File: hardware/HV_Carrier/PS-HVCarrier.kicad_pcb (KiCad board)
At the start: 2 copper layers, 291 parts, among them IC1 LM74502DDFR, IC2 TCAN3413DR, IC3 TCAN3413DR, J1 Shunt Breakout, J10 Shunt Conn, J12 Discharge Vin, J13 Charge Vin, J2 Hall Breakout, J3 IMD_Conn, J4 Voltage Tap, J5 BPS Conn, J6 USB_C_Receptacle_USB2.0_16P, J7 SWD_Header, J8 SWD, J9 LZSR 80-P, Q1 PSMN012-100YS, Q2 PSMN012-100YS, SW1 Reset, SW2 SW_SPDT, U1 MCP1826S, U10 TPS2117DRLR, U11 TLV9002QDRQ1, U12 TLV9002QDRQ1, U13 LMR51635XDDCR, U2 CDSOT23-T24CAN, U3 CDSOT23-T24CAN, U4 AMC3311QDWERQ1, U5 STM32G473CETx, U6 TLV9002QDRQ1, U7 AMC3311QDWERQ1, U8 AMC3311QDWERQ1, U9 AMC3311QDWERQ1, Y1 Crystal

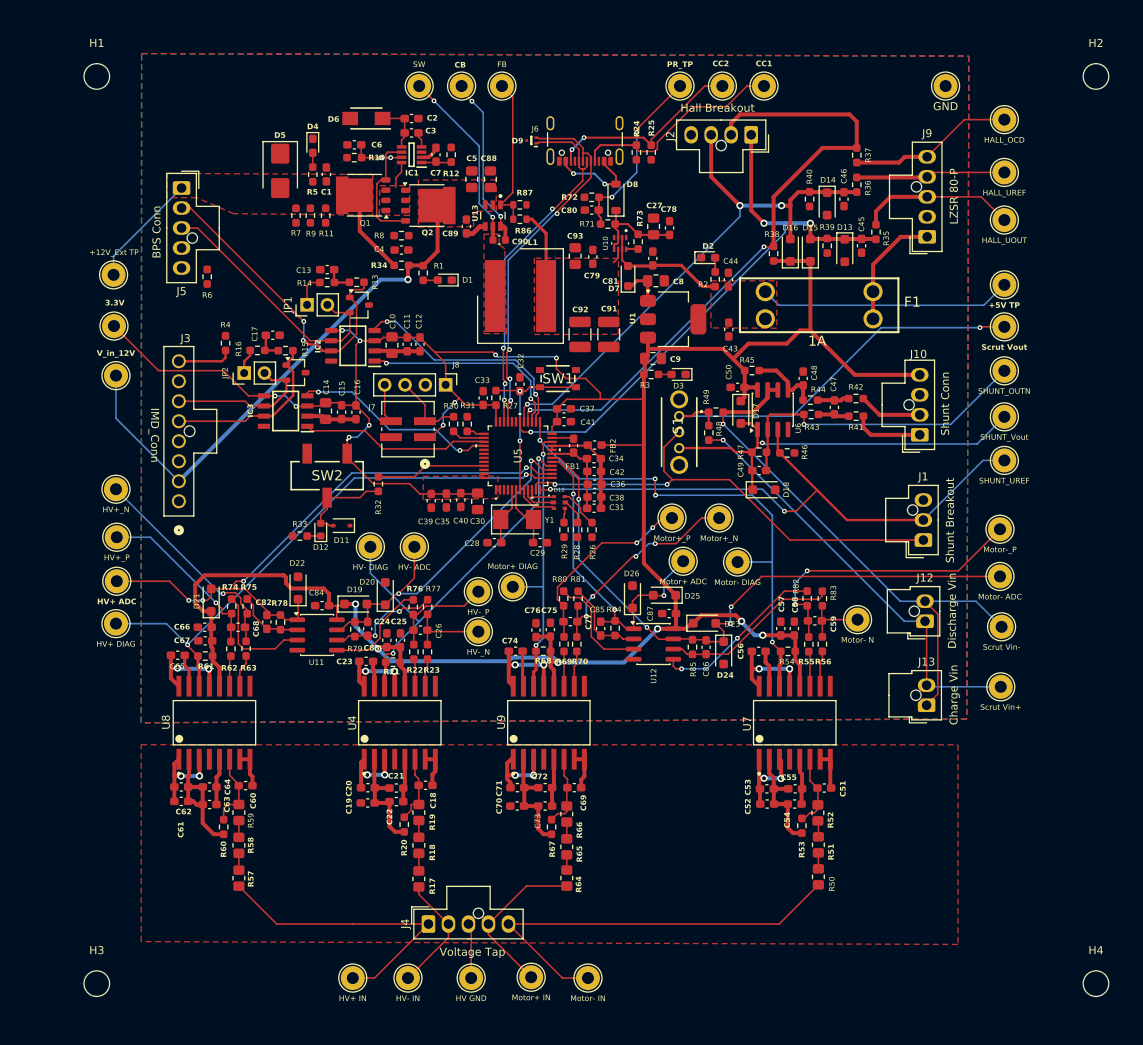
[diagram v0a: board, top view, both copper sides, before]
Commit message: yurrr bang bang
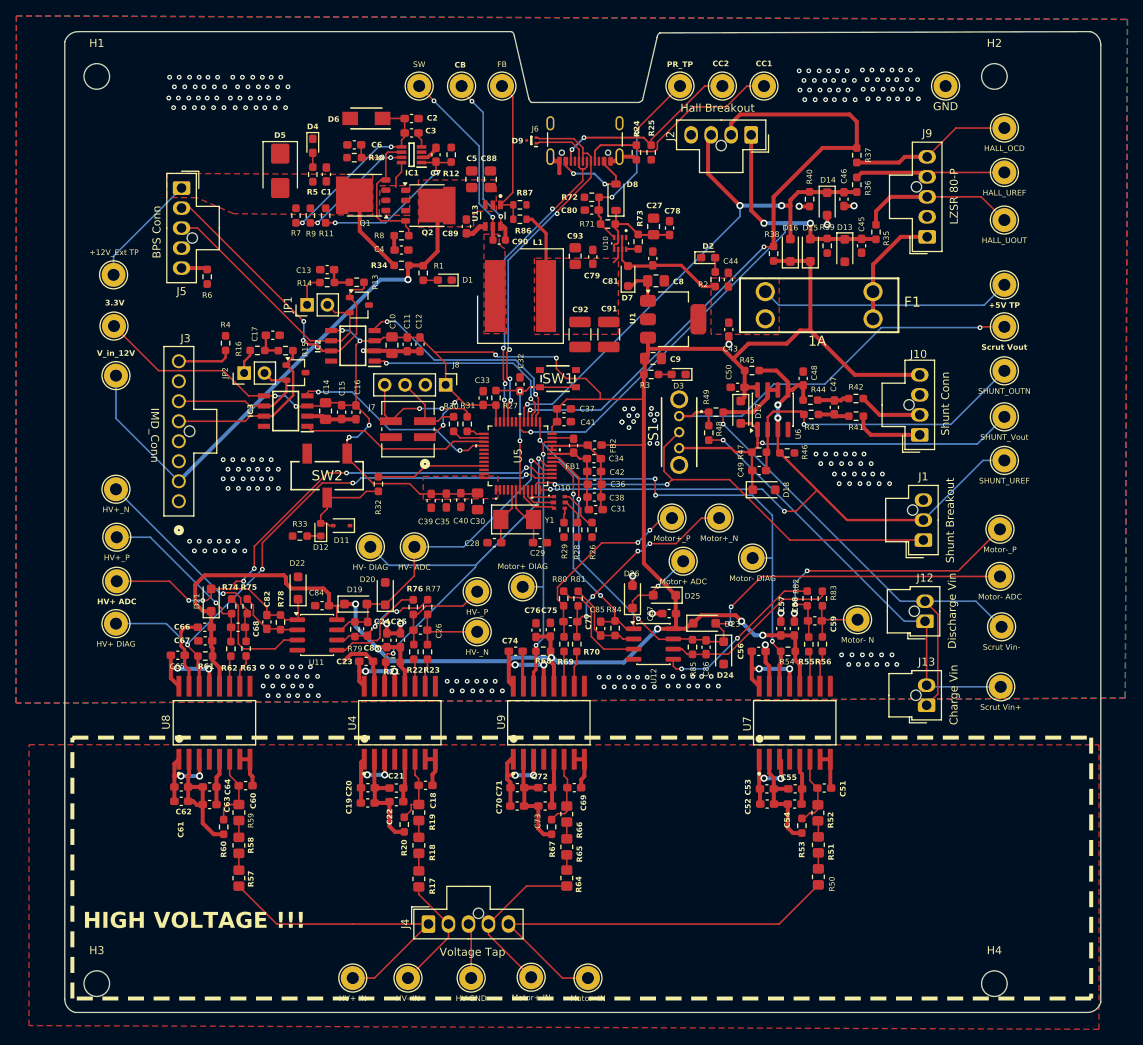
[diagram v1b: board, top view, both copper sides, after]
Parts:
- moved H2 12.7 mm to (185.4, 37.6)
- moved H4 12.7 mm to (185.4, 151.0)
- moved TP34 1.95 mm to (155.2, 97.8)
- moved TP26 1.24 mm to (126.4, 101.4)
- moved TP12 1.05 mm to (186.7, 44.0)
- moved C31 0.27 mm to (135.6, 91.7)
- moved TP30 0.15 mm to (120.8, 107.0)
- moved TP29 0.15 mm to (120.8, 102.0)
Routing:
- net GND: track 36.3 -> 68.4 mm, vias 0 -> 254
- net /Power_Data/PowerProtection/EN/UVLO: track 3.73 -> 21.5 mm, vias 0 -> 2
- net Net-(D6-K): track 6.48 -> 23.6 mm, vias 0 -> 2
- net /Power_Data/PowerProtection/OV: track 6.63 -> 19.0 mm, vias 2 -> 3
- net Net-(J7-Pin_4): track 4.86 -> 15.8 mm, vias 0 -> 2
- net /SHUNT_UREF: track 83.7 -> 89.2 mm, vias 2 -> 4
- net /HV-_ADC: track 45.7 -> 41.1 mm, vias 2 -> 1
- net Net-(J5-SHIELD): track 0.00 -> 3.27 mm
- net /Power_Data/Power_Mux/PR1: track 22.5 -> 24.9 mm
- net Net-(U9-DCDC_OUT): track 9.49 -> 11.8 mm
- net /HV-_DIAG: track 50.9 -> 53.0 mm
- net /HV+_ADC: track 75.9 -> 78.0 mm, vias 4 -> 6
- net /Power_Data/PowerProtection/gate: track 14.5 -> 16.6 mm
- net /HV+_DIAG: track 70.4 -> 72.3 mm, vias 2 -> 4
- net Net-(U4-DCDC_OUT): track 8.69 -> 10.6 mm
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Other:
- board outline added: 129.5 x 122.6 mm
- board text added: "HIGH VOLTAGE !!!"

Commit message: saving silkscreen
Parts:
- added G***: LOGO, LOGO, F.Cu at (181.6, 134.3)
- added G***: LHRs_LOGO, UTSVT_Logos:LHRs_LOGO, F.Cu at (84.4, 45.3)
- added G***: LOGO, LOGO, F.Cu at (189.8, 97.7)
- added G***: LOGO, LOGO, F.Cu at (82.5, 140.5)
- added G***: LOGO, LOGO, B.Cu at (132.9, 75.0)
- moved D1 3.73 mm to (114.0, 65.6), turned to 90 degrees
- moved D2 1.51 mm to (150.5, 59.0), turned to -90 degrees
- moved C89 0.63 mm to (120.0, 56.4)
- moved TP26 0.60 mm to (126.4, 102.0)
- moved C13 0.48 mm to (102.0, 61.3)
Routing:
- net GND: track 68.4 -> 67.6 mm
- net Net-(C13-Pad1): track 3.51 -> 4.05 mm
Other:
- board text added: "12-5 Buck"
- board text added: "9/11/2026"
- board text added: "CAN"
- board text added: "HV Carrier"
- board text added: "Hall Sensor"
- board text added: "LDO"
- board text added: "Power Protection"
- board text added: "Rev A 2026"
- board text added: "Shunt + Scrut"
- board text added: "Shuopu Wang"
- board text added: "Voltage Thang"
